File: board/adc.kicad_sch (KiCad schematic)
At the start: 6 parts, among them U1 ADS131M03, X1 8MhZ

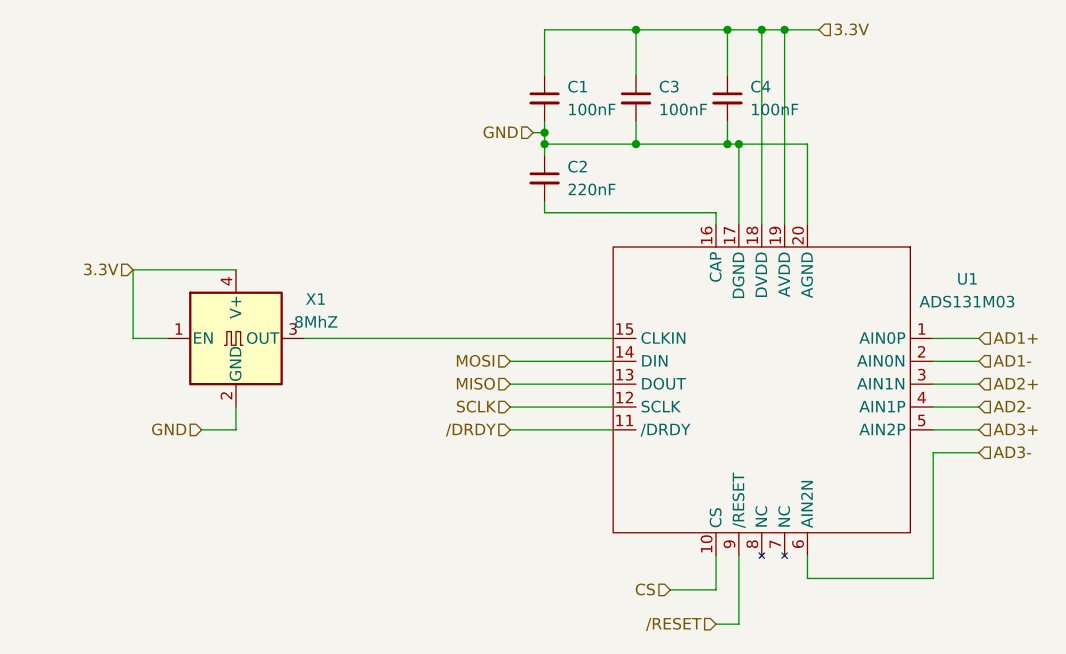
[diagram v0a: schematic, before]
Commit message: added ground pours, a picture and decoupling for the oscillator
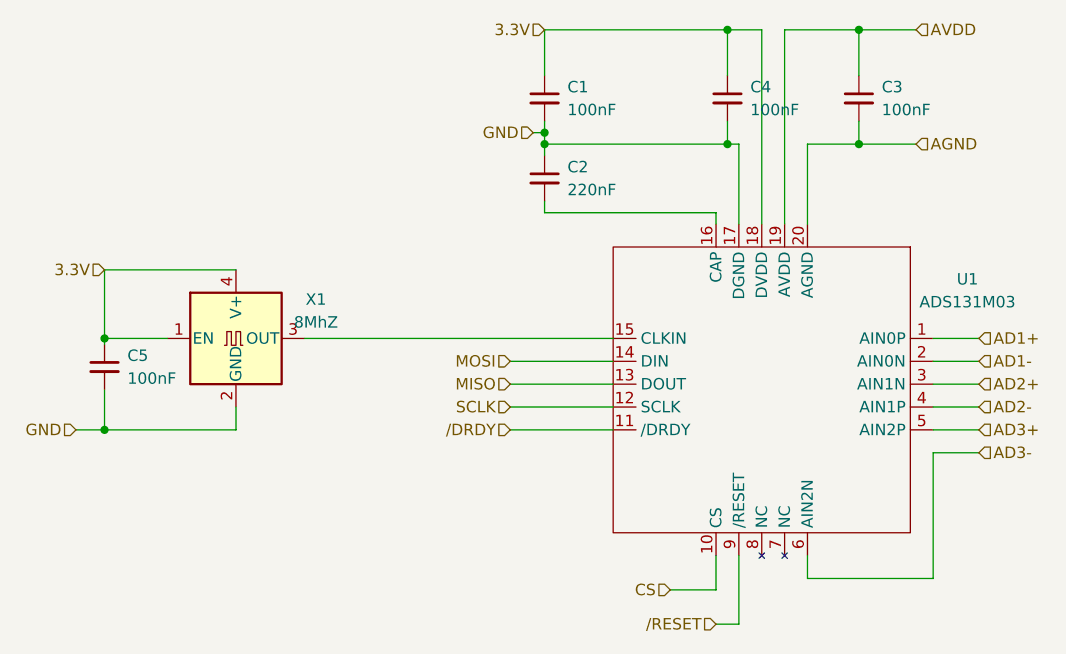
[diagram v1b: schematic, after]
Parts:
- added C5: 100nF, Capacitor_SMD:C_0603_1608Metric, symbol Device:C_Small
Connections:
- net 3.3V: now also C5.1; no longer C3.1, U1.19 (AVDD)
- net GND: now also C5.2; no longer C3.2, U1.20 (AGND)
- new net AGND: C3.2, U1.20 (AGND)
- new net AVDD: C3.1, U1.19 (AVDD)
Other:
- moved on the sheet: C3
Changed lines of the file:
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@@
 (kicad_sch (version 20211123) (generator eeschema)
   (paper "A4")
-  (junction (at 140.97 72.39) (diameter 0) (color 0 0 0 0)
-  )
-  (junction (at 140.97 85.09) (diameter 0) (color 0 0 0 0)
+  (junction (at 81.915 116.84) (diameter 0) (color 0 0 0 0)
   )
   (junction (at 130.81 85.09) (diameter 0) (color 0 0 0 0)
   )
-  (junction (at 157.48 72.39) (diameter 0) (color 0 0 0 0)
-  )
-  (junction (at 152.4 85.09) (diameter 0) (color 0 0 0 0)
-  )
   (junction (at 151.13 85.09) (diameter 0) (color 0 0 0 0)
   )
   (junction (at 130.81 83.82) (diameter 0) (color 0 0 0 0)
   )
-  (junction (at 154.94 72.39) (diameter 0) (color 0 0 0 0)
+  (junction (at 165.735 85.09) (diameter 0) (color 0 0 0 0)
+  )
+  (junction (at 81.915 106.68) (diameter 0) (color 0 0 0 0)
   )
   (junction (at 151.13 72.39) (diameter 0) (color 0 0 0 0)
   )
+  (junction (at 165.735 72.39) (diameter 0) (color 0 0 0 0)
+  )
   (wire (pts (xy 173.99 109.22) (xy 179.07 109.22))
     (stroke (width 0) (type default) (color 0 0 0 0))
   )
-  (wire (pts (xy 154.94 72.39) (xy 157.48 72.39))
-    (stroke (width 0) (type default) (color 0 0 0 0))
-  )
-  (wire (pts (xy 85.09 99.06) (xy 85.09 106.68))
-    (stroke (width 0) (type default) (color 0 0 0 0))
-  )
-  (wire (pts (xy 140.97 72.39) (xy 140.97 77.47))
+  (wire (pts (xy 81.915 99.06) (xy 81.915 106.68))
+    (stroke (width 0) (type default) (color 0 0 0 0))
+  )
+  (wire (pts (xy 81.915 112.395) (xy 81.915 116.84))
     (stroke (width 0) (type default) (color 0 0 0 0))
   )
@@
     (stroke (width 0) (type default) (color 0 0 0 0))
   )
-  (wire (pts (xy 85.09 99.06) (xy 96.52 99.06))
+  (wire (pts (xy 165.735 72.39) (xy 172.085 72.39))
+    (stroke (width 0) (type default) (color 0 0 0 0))
+  )
+  (wire (pts (xy 81.915 106.68) (xy 81.915 107.315))
+    (stroke (width 0) (type default) (color 0 0 0 0))
+  )
+  (wire (pts (xy 81.915 99.06) (xy 96.52 99.06))
     (stroke (width 0) (type default) (color 0 0 0 0))
   )
@@
     (stroke (width 0) (type default) (color 0 0 0 0))
   )
-  (wire (pts (xy 140.97 85.09) (xy 151.13 85.09))
-    (stroke (width 0) (type default) (color 0 0 0 0))
-  )
   (wire (pts (xy 151.13 82.55) (xy 151.13 85.09))
     (stroke (width 0) (type default) (color 0 0 0 0))
@@
     (stroke (width 0) (type default) (color 0 0 0 0))
   )
+  (wire (pts (xy 165.735 77.47) (xy 165.735 72.39))
+    (stroke (width 0) (type default) (color 0 0 0 0))
+  )
   (wire (pts (xy 151.13 72.39) (xy 151.13 77.47))
     (stroke (width 0) (type default) (color 0 0 0 0))
@@
     (stroke (width 0) (type default) (color 0 0 0 0))
   )
-  (wire (pts (xy 140.97 72.39) (xy 151.13 72.39))
+  (wire (pts (xy 130.81 72.39) (xy 151.13 72.39))
     (stroke (width 0) (type default) (color 0 0 0 0))
   )
@@
     (stroke (width 0) (type default) (color 0 0 0 0))
   )
+  (wire (pts (xy 81.915 116.84) (xy 96.52 116.84))
+    (stroke (width 0) (type default) (color 0 0 0 0))
+  )
   (wire (pts (xy 152.4 138.43) (xy 152.4 130.81))
     (stroke (width 0) (type default) (color 0 0 0 0))
@@
     (stroke (width 0) (type default) (color 0 0 0 0))
   )
+  (wire (pts (xy 165.735 85.09) (xy 172.085 85.09))
+    (stroke (width 0) (type default) (color 0 0 0 0))
+  )
   (wire (pts (xy 130.81 83.82) (xy 130.81 82.55))
     (stroke (width 0) (type default) (color 0 0 0 0))
@@
     (stroke (width 0) (type default) (color 0 0 0 0))
   )
+  (wire (pts (xy 160.02 85.09) (xy 165.735 85.09))
+    (stroke (width 0) (type default) (color 0 0 0 0))
+  )
   (wire (pts (xy 127 116.84) (xy 138.43 116.84))
     (stroke (width 0) (type default) (color 0 0 0 0))
@@
     (stroke (width 0) (type default) (color 0 0 0 0))
   )
-  (wire (pts (xy 130.81 72.39) (xy 140.97 72.39))
-    (stroke (width 0) (type default) (color 0 0 0 0))
-  )
   (wire (pts (xy 157.48 72.39) (xy 157.48 93.98))
     (stroke (width 0) (type default) (color 0 0 0 0))
@@
     (stroke (width 0) (type default) (color 0 0 0 0))
   )
-  (wire (pts (xy 157.48 72.39) (xy 161.29 72.39))
+  (wire (pts (xy 157.48 72.39) (xy 165.735 72.39))
+    (stroke (width 0) (type default) (color 0 0 0 0))
+  )
+  (wire (pts (xy 165.735 85.09) (xy 165.735 82.55))
     (stroke (width 0) (type default) (color 0 0 0 0))
   )
@@
     (stroke (width 0) (type default) (color 0 0 0 0))
   )
-  (wire (pts (xy 92.71 116.84) (xy 96.52 116.84))
+  (wire (pts (xy 78.74 116.84) (xy 81.915 116.84))
     (stroke (width 0) (type default) (color 0 0 0 0))
   )
@@
     (stroke (width 0) (type default) (color 0 0 0 0))
   )
-  (wire (pts (xy 152.4 85.09) (xy 160.02 85.09))
-    (stroke (width 0) (type default) (color 0 0 0 0))
-  )
-  (wire (pts (xy 140.97 82.55) (xy 140.97 85.09))
-    (stroke (width 0) (type default) (color 0 0 0 0))
-  )
-  (wire (pts (xy 88.9 106.68) (xy 85.09 106.68))
+  (wire (pts (xy 81.915 106.68) (xy 88.9 106.68))
     (stroke (width 0) (type default) (color 0 0 0 0))
   )
@@
     (stroke (width 0) (type default) (color 0 0 0 0))
   )
-  (wire (pts (xy 140.97 85.09) (xy 130.81 85.09))
+  (wire (pts (xy 130.81 85.09) (xy 151.13 85.09))
     (stroke (width 0) (type default) (color 0 0 0 0))
   )
@@
     (effects (font (size 1.27 1.27)) (justify right))
   )
-  (hierarchical_label "3.3V" (shape input) (at 85.09 99.06 180)
+  (hierarchical_label "3.3V" (shape input) (at 81.915 99.06 180)
     (effects (font (size 1.27 1.27)) (justify right))
   )
@@
     (effects (font (size 1.27 1.27)) (justify right))
   )
-  (hierarchical_label "GND" (shape input) (at 92.71 116.84 180)
+  (hierarchical_label "AGND" (shape input) (at 172.085 85.09 0)
+    (effects (font (size 1.27 1.27)) (justify left))
+  )
+  (hierarchical_label "GND" (shape input) (at 78.74 116.84 180)
     (effects (font (size 1.27 1.27)) (justify right))
   )
@@
     (effects (font (size 1.27 1.27)) (justify left))
   )
-  (hierarchical_label "3.3V" (shape input) (at 161.29 72.39 0)
-    (effects (font (size 1.27 1.27)) (justify left))
+  (hierarchical_label "3.3V" (shape input) (at 130.81 72.39 180)
+    (effects (font (size 1.27 1.27)) (justify right))
   )
   (hierarchical_label "GND" (shape input) (at 129.54 83.82 180)
     (effects (font (size 1.27 1.27)) (justify right))
+  )
+  (hierarchical_label "AVDD" (shape input) (at 172.085 72.39 0)
+    (effects (font (size 1.27 1.27)) (justify left))
   )
   (hierarchical_label "CS" (shape input) (at 144.78 134.62 180)
@@
     (pin "4")
   )
-  (symbol (lib_id "Device:C_Small") (at 140.97 80.01 0) (unit 1)
-    (in_bom yes) (on_board yes) (fields_autoplaced)
-    (property "Reference" "C3" (id 0) (at 143.51 78.7462 0)
-      (effects (font (size 1.27 1.27)) (justify left))
-    )
-    (property "Value" "100nF" (id 1) (at 143.51 81.2862 0)
-      (effects (font (size 1.27 1.27)) (justify left))
-    )
-    (property "Footprint" "Capacitor_SMD:C_0603_1608Metric" (id 2) (at 140.97 80.01 0)
-      (effects (font (size 1.27 1.27)) hide)
-    )
-    (property "Datasheet" "~" (id 3) (at 140.97 80.01 0)
+  (symbol (lib_id "Device:C_Small") (at 165.735 80.01 0) (unit 1)
+    (in_bom yes) (on_board yes) (fields_autoplaced)
+    (property "Reference" "C3" (id 0) (at 168.275 78.7462 0)
+      (effects (font (size 1.27 1.27)) (justify left))
+    )
+    (property "Value" "100nF" (id 1) (at 168.275 81.2862 0)
+      (effects (font (size 1.27 1.27)) (justify left))
+    )
+    (property "Footprint" "Capacitor_SMD:C_0603_1608Metric" (id 2) (at 165.735 80.01 0)
+      (effects (font (size 1.27 1.27)) hide)
+    )
+    (property "Datasheet" "~" (id 3) (at 165.735 80.01 0)
       (effects (font (size 1.27 1.27)) hide)
     )
@@
       (effects (font (size 1.27 1.27)) hide)
     )
+    (pin "1")
+    (pin "2")
+  )
+  (symbol (lib_id "Device:C_Small") (at 81.915 109.855 0) (unit 1)
+    (in_bom yes) (on_board yes) (fields_autoplaced)
+    (property "Reference" "C5" (id 0) (at 84.455 108.5912 0)
+      (effects (font (size 1.27 1.27)) (justify left))
+    )
+    (property "Value" "100nF" (id 1) (at 84.455 111.1312 0)
+      (effects (font (size 1.27 1.27)) (justify left))
+    )
+    (property "Footprint" "Capacitor_SMD:C_0603_1608Metric" (id 2) (at 81.915 109.855 0)
+      (effects (font (size 1.27 1.27)) hide)
+    )
+    (property "Datasheet" "~" (id 3) (at 81.915 109.855 0)
+      (effects (font (size 1.27 1.27)) hide)
+    )
